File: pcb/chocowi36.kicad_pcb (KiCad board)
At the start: 2 copper layers, 113.2 x 88.5 mm, 27 parts, among them SW10 SW_Push, SW11 SW_Push, SW12 SW_Push, SW14 SW_Push, SW15 SW_Push, SW16 SW_Push, SW17 SW_Push, SW18 SW_Push, SW19 SW_Push, SW2 SW_Push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

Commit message: small changes + update doc
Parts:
- removed H2, H3: MountingHole, itsdmd:MountingHole_1.6mm_M1.4
- added ?: , , F.Cu at (103.9, 105.0)
- added ?: , , F.Cu at (150.6, 51.0)
- H1, H4: footprint itsdmd:MountingHole_1.6mm_M1.4 -> itsdmd:MountingHole_2.2mm_M2
- moved H1 13.3 mm to (90.5, 55.0)
- moved H4 12.9 mm to (178.6, 111.3)
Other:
- board size 113.2 x 88.5 mm -> 113.1 x 88.3 mm
- board text added: "by itsdmd"
- board text added: "chocowi36"

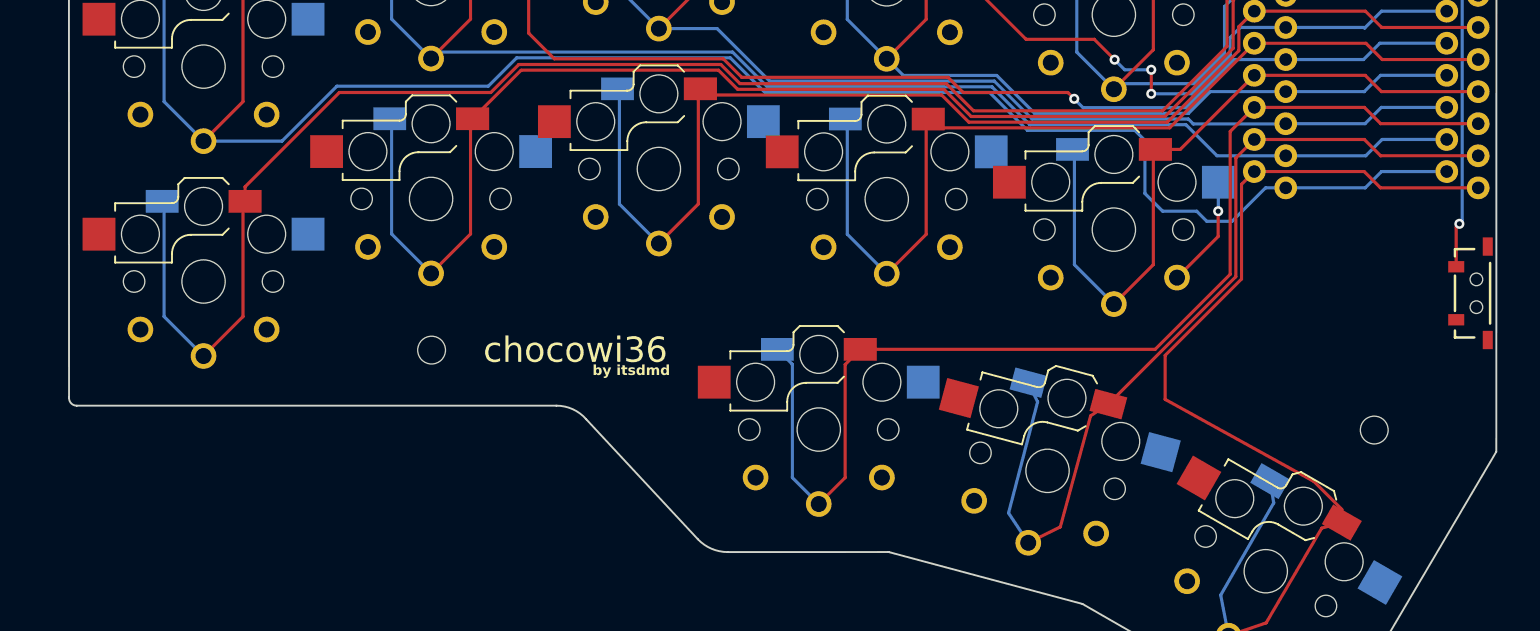
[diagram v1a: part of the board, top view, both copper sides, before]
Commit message: adjust thumb cluster
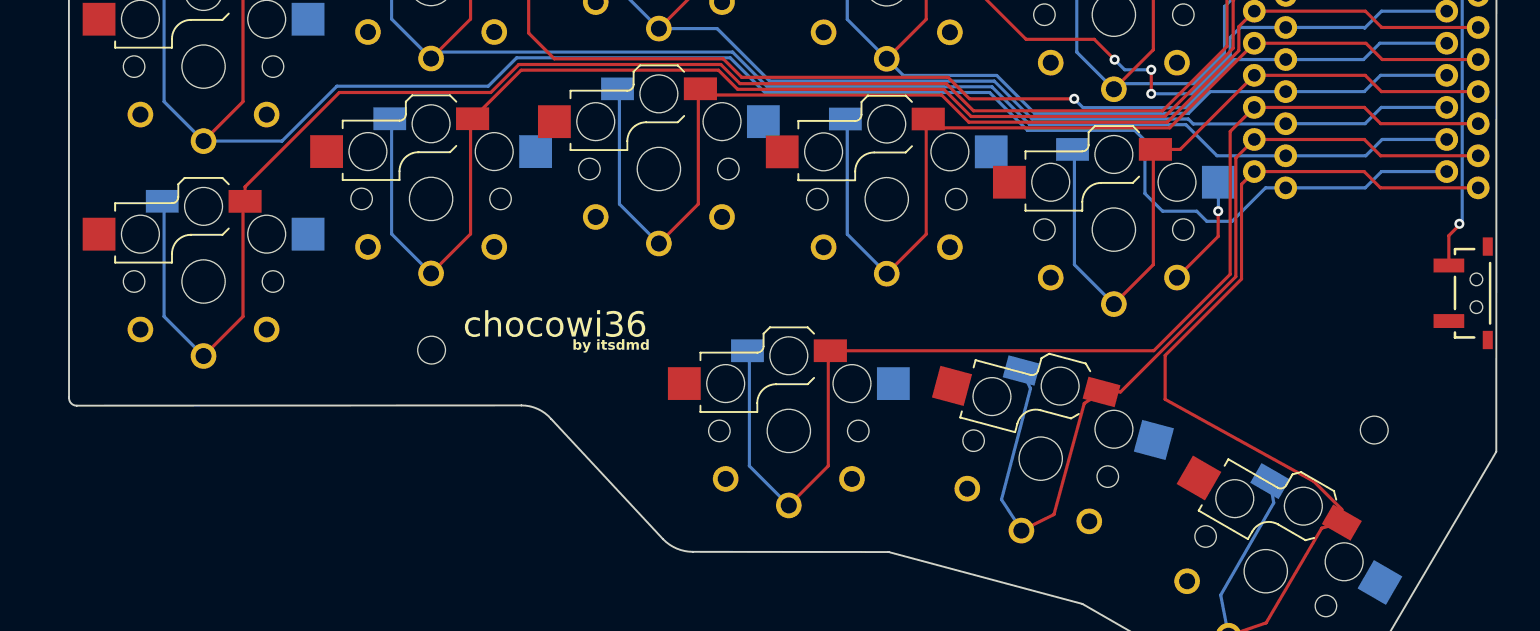
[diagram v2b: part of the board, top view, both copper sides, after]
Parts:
- moved SW19 2.37 mm to (132.2, 111.4)
- moved SW20 1.11 mm to (152.1, 113.6)
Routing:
- net Switch19: track 91.2 -> 93.7 mm
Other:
- outline, holes or cut-outs redrawn

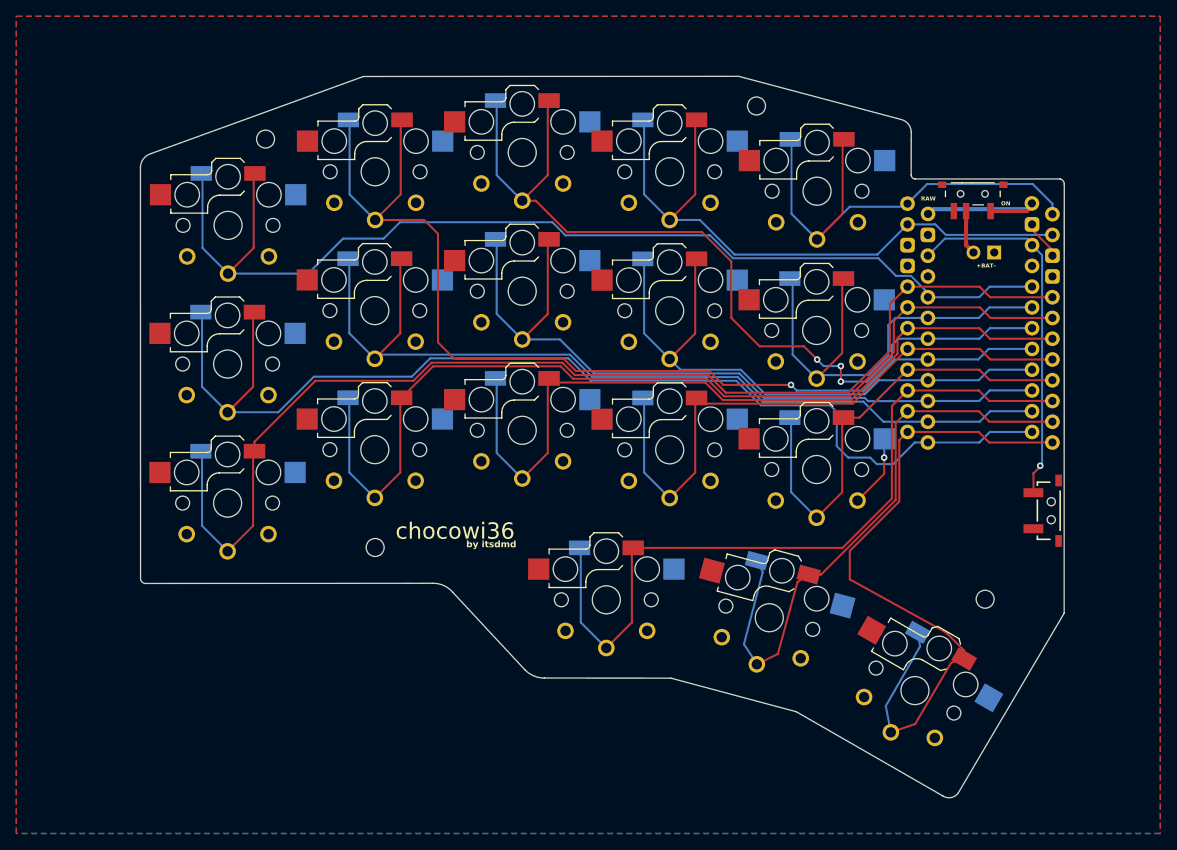
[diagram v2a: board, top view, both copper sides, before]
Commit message: fix thumb cluster
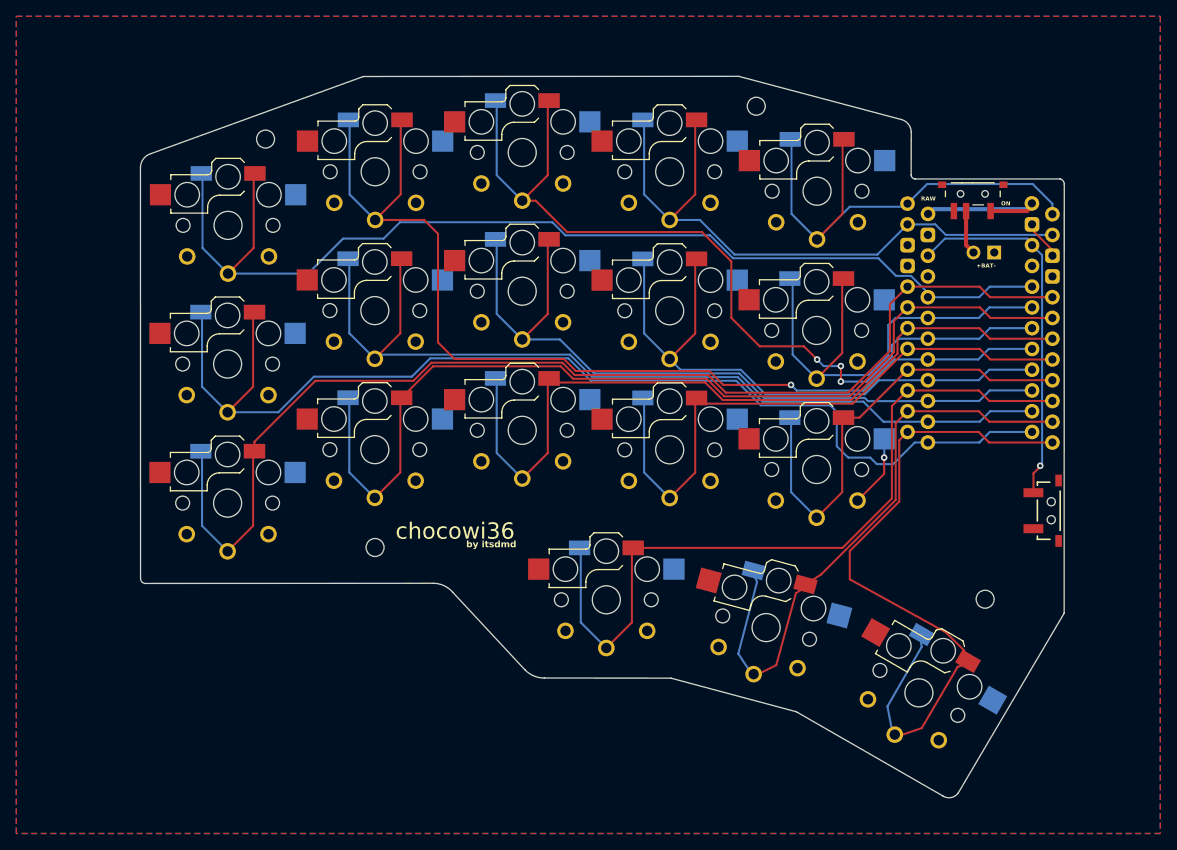
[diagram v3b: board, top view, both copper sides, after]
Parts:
- removed ? (x2): , 
- added H2: MountingHole, itsdmd:MountingHole_2.2mm_M2, F.Cu at (103.9, 105.0)
- added H3: MountingHole, itsdmd:MountingHole_2.2mm_M2, F.Cu at (150.6, 51.0)
- moved SW20 1.27 mm to (151.8, 114.8)
- moved SW21 0.56 mm to (170.4, 122.8)
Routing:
- net Switch20: track 71.4 -> 72.1 mm

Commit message: update routing to support placing tactile switches on both sides
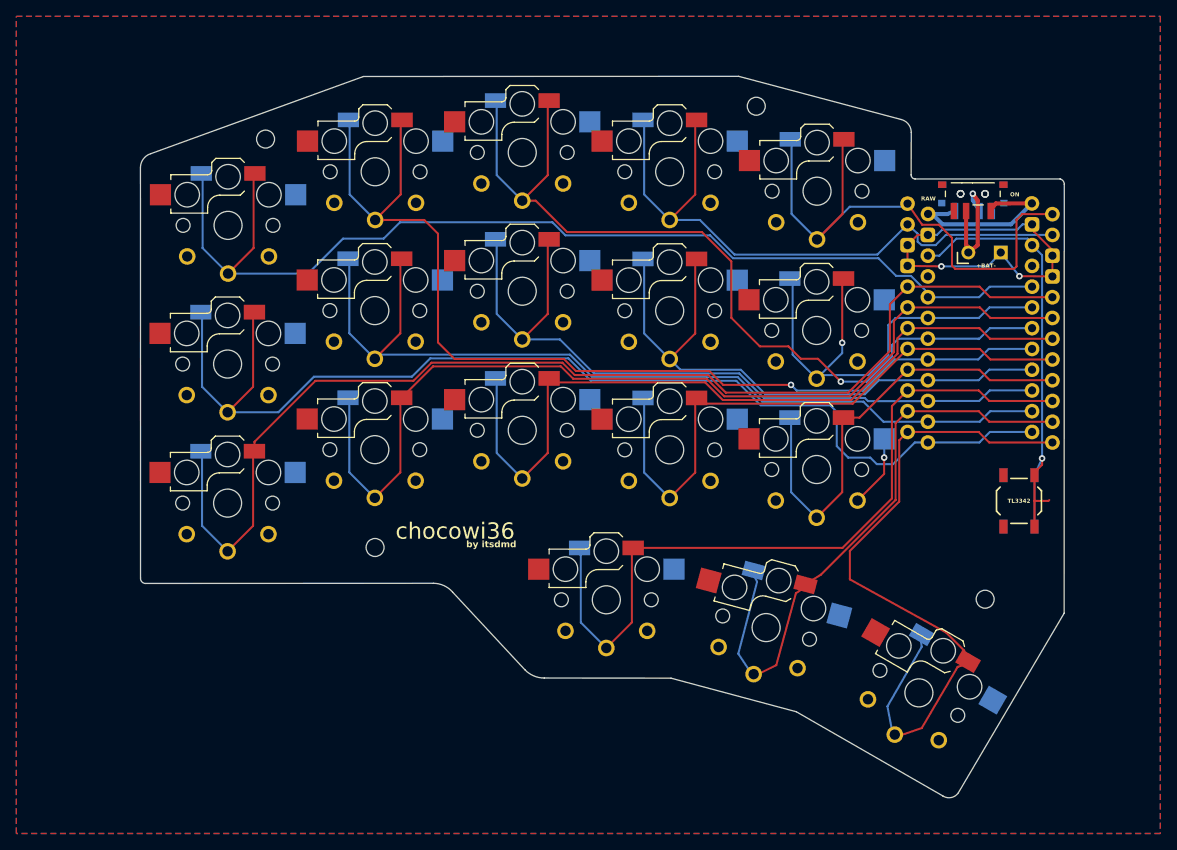
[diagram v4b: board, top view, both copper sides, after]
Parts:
- added SW_POWER2: SW_SPDT, itsdmd:SW-S_MSK-12C02, B.Cu at (176.9, 61.7)
- added SW_RST2: SW_Push, itsdmd:SW-T_SPST_TL3342, B.Cu at (182.7, 99.3)
- SW_RST1: footprint itsdmd:SW-T_7.4x2.6-4pad-smd -> itsdmd:SW-T_SPST_TL3342
- moved SW_RST1 4.22 mm to (182.7, 99.3)
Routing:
- net gnd: track 15.2 -> 55.8 mm, vias 1 -> 3
- net reset: track 45.4 -> 59.8 mm
- net Net-(BT1-+): track 5.45 -> 15.7 mm, vias 0 -> 1
- net Switch6: track 61.1 -> 69.5 mm
- net +BATT: track 19.1 -> 23.2 mm
- net Switch5: track 77.6 -> 79.4 mm
- net Switch19: track 93.7 -> 94.9 mm
- net Switch4: track 107.5 -> 106.4 mm, vias 3 -> 1
- net Switch12: vias 0 -> 1
